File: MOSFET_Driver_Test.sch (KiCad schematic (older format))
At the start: 20 parts, among them U1 FD6288Q

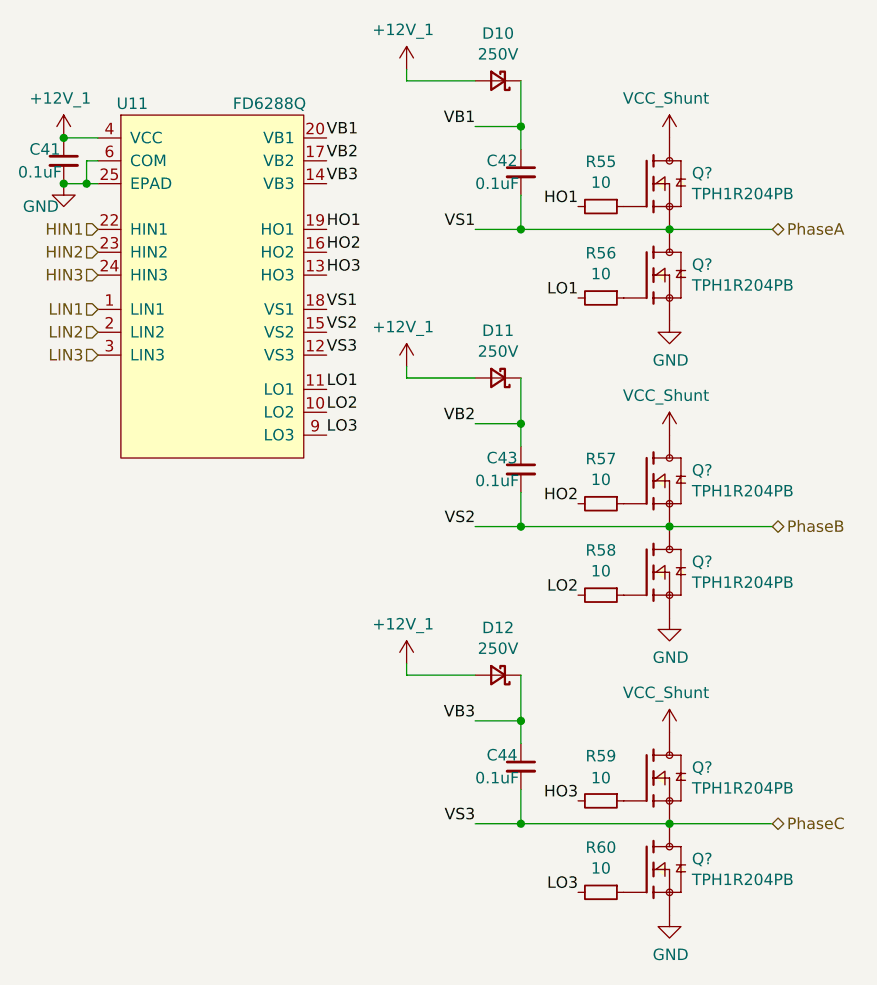
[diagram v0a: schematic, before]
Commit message: Lots of changes made with back being rerouted
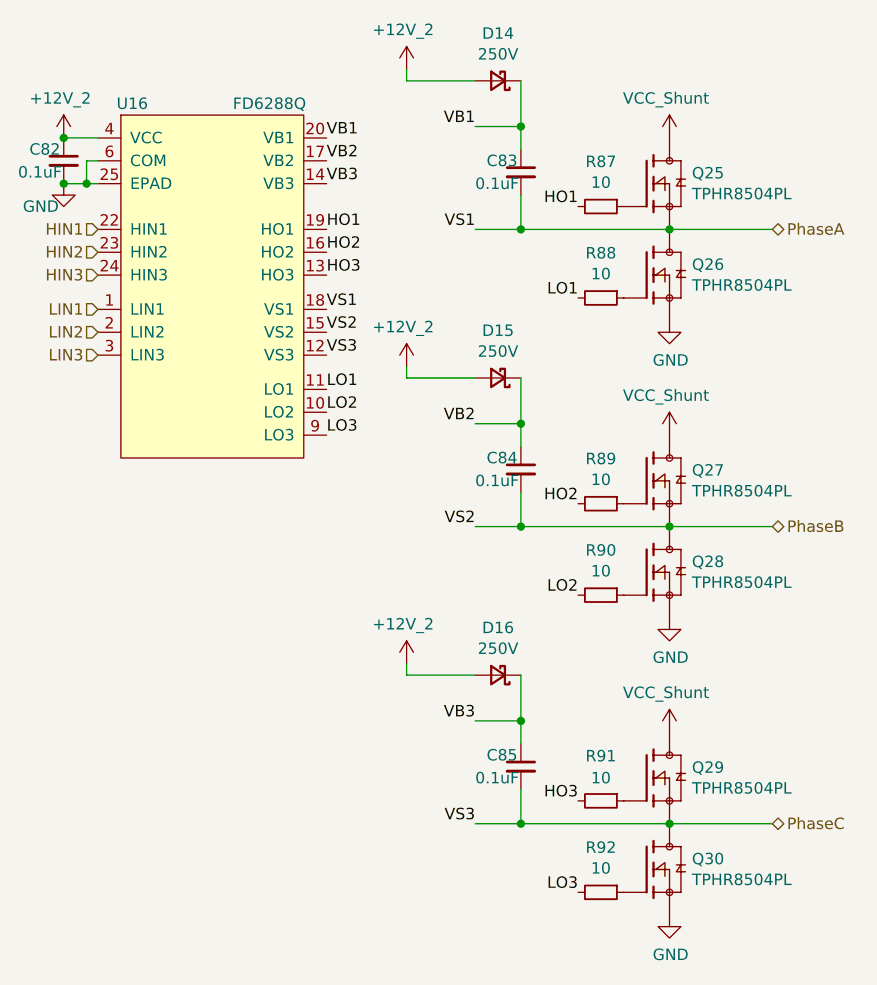
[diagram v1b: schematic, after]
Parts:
- removed Q? (x6): TPH1R204PB, Footprints:TPH1R204PB, symbol JPW_Symbols:TPH1R204PB
- added Q1, Q2, Q3, Q4, Q5, Q6: TPHR8504PL, Footprints:TPHR8504PL, symbol JPW_Symbols:TPHR8504PL
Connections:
- net GND: now also Q2.1, Q2.2, Q2.3, Q4.1, Q4.2, Q4.3, Q6.1, Q6.2, Q6.3
- net PhaseA: now also Q1.1, Q1.2, Q1.3, Q2.5, Q2.6, Q2.7, Q2.8, Q2.9
- net PhaseB: now also Q3.1, Q3.2, Q3.3, Q4.5, Q4.6, Q4.7, Q4.8, Q4.9
- net PhaseC: now also Q5.1, Q5.2, Q5.3, Q6.5, Q6.6, Q6.7, Q6.8, Q6.9
- net VCC_Shunt: now also Q1.5, Q1.6, Q1.7, Q1.8, Q1.9, Q3.5, Q3.6, Q3.7, Q3.8, Q3.9, Q5.5, Q5.6, Q5.7, Q5.8, Q5.9
- net at R8.1: now also Q2.4
- net at R7.1: now also Q1.4
- net at R10.1: now also Q4.4
- net at R12.1: now also Q6.4
- net at R11.1: now also Q5.4
- net at R9.1: now also Q3.4
- net +12V_1 renamed +12V_2
